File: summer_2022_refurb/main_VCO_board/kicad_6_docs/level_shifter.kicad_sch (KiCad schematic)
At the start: 5 parts

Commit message: Main VCO progress
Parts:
- removed R?: 100k, symbol Device:R
- R?: value 100k -> 33k
- R?: value 200k -> 100k
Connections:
- net GND: now also R?.1; no longer U?.3 (+)
- net IN: now also U?.3 (+); no longer R?.1
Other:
- note added: "Upgoing sawtooth [-1.25, +1.25v]"
- note added: "upgoing sawtooth [-5v, +5v]"
- note removed: "[-1.25, +1.25v] in"
- note removed: "[-5v, +5v] out"
- title: (none) -> Josh Ox Ribon Synth Main VCO board
- moved on the sheet: R?
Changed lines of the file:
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@@
 (kicad_sch (version 20211123) (generator eeschema)
   (paper "A4")
+  (title_block
+    (title "Josh Ox Ribon Synth Main VCO board")
+    (date "2022-06-18")
+    (rev "0")
+    (comment 2 "creativecommons.org/licences/by/4.0")
+    (comment 3 "license: CC by 4.0")
+    (comment 4 "Author: Jordan Acete")
+  )
   (junction (at 161.29 101.6) (diameter 0) (color 0 0 0 0)
   )
   (junction (at 161.29 91.44) (diameter 0) (color 0 0 0 0)
   )
-  (junction (at 135.89 101.6) (diameter 0) (color 0 0 0 0)
-  )
-  (junction (at 123.19 101.6) (diameter 0) (color 0 0 0 0)
-  )
-  (junction (at 140.97 101.6) (diameter 0) (color 0 0 0 0)
+  (junction (at 140.97 86.36) (diameter 0) (color 0 0 0 0)
   )
   (junction (at 140.97 91.44) (diameter 0) (color 0 0 0 0)
   )
-  (wire (pts (xy 135.89 96.52) (xy 135.89 101.6))
+  (wire (pts (xy 125.73 88.9) (xy 125.73 86.36))
     (stroke (width 0) (type default) (color 0 0 0 0))
   )
@@
     (stroke (width 0) (type default) (color 0 0 0 0))
   )
-  (wire (pts (xy 161.29 91.44) (xy 161.29 101.6))
+  (wire (pts (xy 135.89 86.36) (xy 140.97 86.36))
     (stroke (width 0) (type default) (color 0 0 0 0))
   )
-  (wire (pts (xy 135.89 101.6) (xy 140.97 101.6))
+  (wire (pts (xy 161.29 91.44) (xy 161.29 101.6))
     (stroke (width 0) (type default) (color 0 0 0 0))
   )
@@
     (stroke (width 0) (type default) (color 0 0 0 0))
   )
-  (wire (pts (xy 140.97 109.22) (xy 140.97 106.68))
-    (stroke (width 0) (type default) (color 0 0 0 0))
-  )
   (wire (pts (xy 140.97 101.6) (xy 143.51 101.6))
     (stroke (width 0) (type default) (color 0 0 0 0))
   )
-  (wire (pts (xy 123.19 101.6) (xy 123.19 96.52))
-    (stroke (width 0) (type default) (color 0 0 0 0))
-  )
-  (wire (pts (xy 140.97 80.01) (xy 140.97 91.44))
+  (wire (pts (xy 140.97 80.01) (xy 140.97 86.36))
     (stroke (width 0) (type default) (color 0 0 0 0))
   )
@@
     (stroke (width 0) (type default) (color 0 0 0 0))
   )
-  (wire (pts (xy 140.97 106.68) (xy 143.51 106.68))
+  (wire (pts (xy 105.41 106.68) (xy 143.51 106.68))
     (stroke (width 0) (type default) (color 0 0 0 0))
   )
-  (wire (pts (xy 133.35 106.68) (xy 135.89 106.68))
-    (stroke (width 0) (type default) (color 0 0 0 0))
-  )
-  (wire (pts (xy 95.25 101.6) (xy 123.19 101.6))
+  (wire (pts (xy 140.97 86.36) (xy 140.97 91.44))
     (stroke (width 0) (type default) (color 0 0 0 0))
   )
@@
     (stroke (width 0) (type default) (color 0 0 0 0))
   )
-  (wire (pts (xy 135.89 101.6) (xy 135.89 106.68))
-    (stroke (width 0) (type default) (color 0 0 0 0))
-  )
-  (wire (pts (xy 161.29 101.6) (xy 187.96 101.6))
+  (wire (pts (xy 161.29 101.6) (xy 195.58 101.6))
     (stroke (width 0) (type default) (color 0 0 0 0))
   )
@@
     (stroke (width 0) (type default) (color 0 0 0 0))
   )
-  (wire (pts (xy 125.73 106.68) (xy 123.19 106.68))
+  (wire (pts (xy 125.73 86.36) (xy 128.27 86.36))
     (stroke (width 0) (type default) (color 0 0 0 0))
   )
-  (wire (pts (xy 133.35 96.52) (xy 135.89 96.52))
-    (stroke (width 0) (type default) (color 0 0 0 0))
-  )
-  (wire (pts (xy 123.19 96.52) (xy 125.73 96.52))
-    (stroke (width 0) (type default) (color 0 0 0 0))
-  )
-  (wire (pts (xy 123.19 106.68) (xy 123.19 101.6))
-    (stroke (width 0) (type default) (color 0 0 0 0))
-  )
-  (text "[-1.25, +1.25v] in" (at 91.44 99.06 0)
+  (text "Upgoing sawtooth [-1.25, +1.25v]" (at 101.6 104.14 0)
     (effects (font (size 1.27 1.27)) (justify left bottom))
   )
-  (text "[-5v, +5v] out" (at 177.8 99.06 0)
+  (text "upgoing sawtooth [-5v, +5v]" (at 171.45 99.06 0)
     (effects (font (size 1.27 1.27)) (justify left bottom))
   )
-  (hierarchical_label "IN" (shape input) (at 95.25 101.6 180)
+  (hierarchical_label "IN" (shape input) (at 105.41 106.68 180)
     (effects (font (size 1.27 1.27)) (justify right))
   )
-  (hierarchical_label "OUT" (shape output) (at 187.96 101.6 0)
+  (hierarchical_label "OUT" (shape output) (at 195.58 101.6 0)
     (effects (font (size 1.27 1.27)) (justify left))
-  )
-  (symbol (lib_id "power:GND") (at 140.97 109.22 0) (unit 1)
-    (in_bom yes) (on_board yes) (fields_autoplaced)
-    (property "Reference" "#PWR?" (id 0) (at 140.97 115.57 0)
-      (effects (font (size 1.27 1.27)) hide)
-    )
-    (property "Value" "GND" (id 1) (at 140.97 114.3 0))
-    (property "Footprint" "" (id 2) (at 140.97 109.22 0)
-      (effects (font (size 1.27 1.27)) hide)
-    )
-    (property "Datasheet" "" (id 3) (at 140.97 109.22 0)
-      (effects (font (size 1.27 1.27)) hide)
-    )
-    (pin "1")
   )
   (symbol (lib_id "Amplifier_Operational:TL072") (at 151.13 104.14 0) (mirror x) (unit 1)
@@
     (pin "8")
   )
-  (symbol (lib_id "Device:R") (at 129.54 96.52 90) (unit 1)
+  (symbol (lib_id "Device:R") (at 132.08 86.36 90) (unit 1)
     (in_bom yes) (on_board yes) (fields_autoplaced)
-    (property "Reference" "R?" (id 0) (at 129.54 90.17 90))
-    (property "Value" "100k" (id 1) (at 129.54 92.71 90))
-    (property "Footprint" "" (id 2) (at 129.54 98.298 90)
+    (property "Reference" "R?" (id 0) (at 132.08 80.01 90))
+    (property "Value" "33k" (id 1) (at 132.08 82.55 90))
+    (property "Footprint" "" (id 2) (at 132.08 88.138 90)
       (effects (font (size 1.27 1.27)) hide)
     )
-    (property "Datasheet" "~" (id 3) (at 129.54 96.52 0)
+    (property "Datasheet" "~" (id 3) (at 132.08 86.36 0)
       (effects (font (size 1.27 1.27)) hide)
     )
     (pin "1")
     (pin "2")
+  )
+  (symbol (lib_id "power:GND") (at 125.73 88.9 0) (unit 1)
+    (in_bom yes) (on_board yes) (fields_autoplaced)
+    (property "Reference" "#PWR?" (id 0) (at 125.73 95.25 0)
+      (effects (font (size 1.27 1.27)) hide)
+    )
+    (property "Value" "GND" (id 1) (at 125.73 93.98 0))
+    (property "Footprint" "" (id 2) (at 125.73 88.9 0)
+      (effects (font (size 1.27 1.27)) hide)
+    )
+    (property "Datasheet" "" (id 3) (at 125.73 88.9 0)
+      (effects (font (size 1.27 1.27)) hide)
+    )
+    (pin "1")
   )
   (symbol (lib_id "Device:C") (at 151.13 80.01 90) (unit 1)
@@
     (pin "2")
   )
-  (symbol (lib_id "Device:R") (at 129.54 106.68 90) (unit 1)
-    (in_bom yes) (on_board yes) (fields_autoplaced)
-    (property "Reference" "R?" (id 0) (at 129.54 100.33 90))
-    (property "Value" "100k" (id 1) (at 129.54 102.87 90))
-    (property "Footprint" "" (id 2) (at 129.54 108.458 90)
-      (effects (font (size 1.27 1.27)) hide)
-    )
-    (property "Datasheet" "~" (id 3) (at 129.54 106.68 0)
-      (effects (font (size 1.27 1.27)) hide)
-    )
-    (pin "1")
-    (pin "2")
-  )
   (symbol (lib_id "Device:R") (at 151.13 91.44 90) (unit 1)
     (in_bom yes) (on_board yes) (fields_autoplaced)
     (property "Reference" "R?" (id 0) (at 151.13 85.09 90))
-    (property "Value" "200k" (id 1) (at 151.13 87.63 90))
+    (property "Value" "100k" (id 1) (at 151.13 87.63 90))
     (property "Footprint" "" (id 2) (at 151.13 93.218 90)
       (effects (font (size 1.27 1.27)) hide)

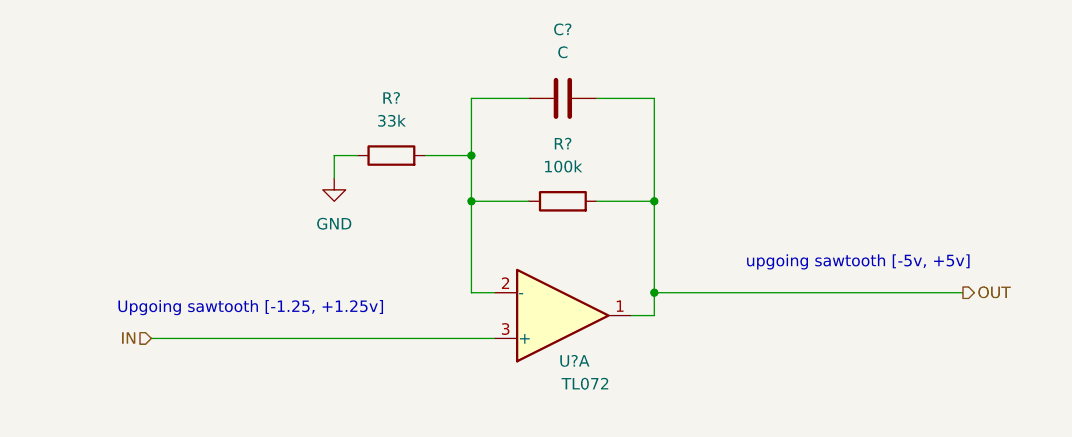
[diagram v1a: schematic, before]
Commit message: Progress on main VCO, schem getting close but not done
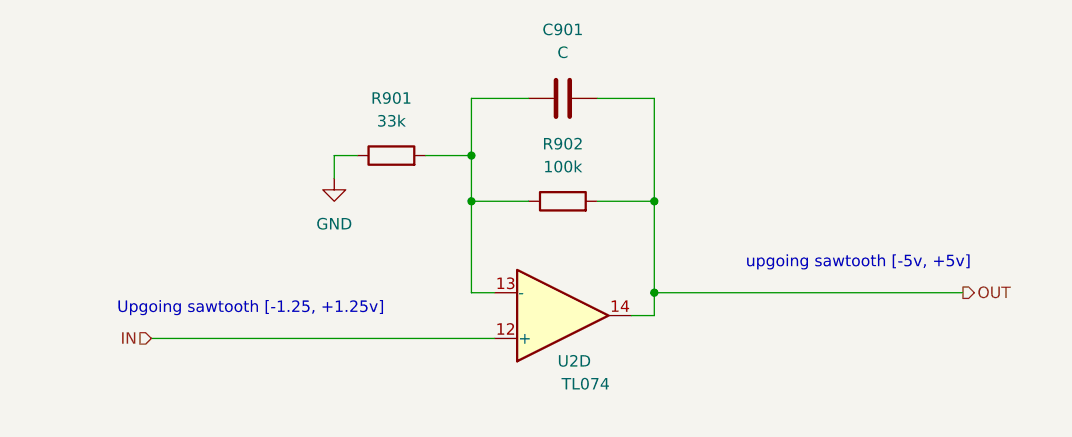
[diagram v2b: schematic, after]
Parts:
- removed U?: TL072, symbol Amplifier_Operational:TL072
- added U2: TL074, symbol Amplifier_Operational:TL074
- gave numbers to parts that had none: 3
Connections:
- net IN: now also U2.12 (+)
- net OUT: now also U2.14
- net at C901.1, R901.2, R902.1: now also U2.13 (-)
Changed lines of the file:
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@@
     (effects (font (size 1.27 1.27)) (justify left))
-  )
-  (symbol (lib_id "Amplifier_Operational:TL072") (at 151.13 104.14 0) (mirror x) (unit 1)
-    (in_bom yes) (on_board yes)
-    (property "Reference" "U?" (id 0) (at 152.4 109.22 0))
-    (property "Value" "TL072" (id 1) (at 153.67 111.76 0))
-    (property "Footprint" "" (id 2) (at 151.13 104.14 0)
-      (effects (font (size 1.27 1.27)) hide)
-    )
-    (property "Datasheet" "http://www.ti.com/lit/ds/symlink/tl071.pdf" (id 3) (at 151.13 104.14 0)
-      (effects (font (size 1.27 1.27)) hide)
-    )
-    (pin "1")
-    (pin "2")
-    (pin "3")
-    (pin "5")
-    (pin "6")
-    (pin "7")
-    (pin "4")
-    (pin "8")
   )
   (symbol (lib_id "Device:R") (at 132.08 86.36 90) (unit 1)
     (in_bom yes) (on_board yes) (fields_autoplaced)
-    (property "Reference" "R?" (id 0) (at 132.08 80.01 90))
+    (property "Reference" "R901" (id 0) (at 132.08 80.01 90))
     (property "Value" "33k" (id 1) (at 132.08 82.55 90))
     (property "Footprint" "" (id 2) (at 132.08 88.138 90)
@@
     (pin "2")
   )
+  (symbol (lib_id "Amplifier_Operational:TL074") (at 151.13 104.14 0) (mirror x) (unit 4)
+    (in_bom yes) (on_board yes)
+    (property "Reference" "U2" (id 0) (at 152.4 109.22 0))
+    (property "Value" "TL074" (id 1) (at 153.67 111.76 0))
+    (property "Footprint" "" (id 2) (at 149.86 106.68 0)
+      (effects (font (size 1.27 1.27)) hide)
+    )
+    (property "Datasheet" "http://www.ti.com/lit/ds/symlink/tl071.pdf" (id 3) (at 152.4 109.22 0)
+      (effects (font (size 1.27 1.27)) hide)
+    )
+    (pin "1")
+    (pin "2")
+    (pin "3")
+    (pin "5")
+    (pin "6")
+    (pin "7")
+    (pin "10")
+    (pin "8")
+    (pin "9")
+    (pin "12")
+    (pin "13")
+    (pin "14")
+    (pin "11")
+    (pin "4")
+  )
   (symbol (lib_id "power:GND") (at 125.73 88.9 0) (unit 1)
     (in_bom yes) (on_board yes) (fields_autoplaced)
-    (property "Reference" "#PWR?" (id 0) (at 125.73 95.25 0)
+    (property "Reference" "#PWR0901" (id 0) (at 125.73 95.25 0)
       (effects (font (size 1.27 1.27)) hide)
     )
@@
   (symbol (lib_id "Device:C") (at 151.13 80.01 90) (unit 1)
     (in_bom yes) (on_board yes) (fields_autoplaced)
-    (property "Reference" "C?" (id 0) (at 151.13 72.39 90))
+    (property "Reference" "C901" (id 0) (at 151.13 72.39 90))
     (property "Value" "C" (id 1) (at 151.13 74.93 90))
     (property "Footprint" "" (id 2) (at 154.94 79.0448 0)
@@
   (symbol (lib_id "Device:R") (at 151.13 91.44 90) (unit 1)
     (in_bom yes) (on_board yes) (fields_autoplaced)
-    (property "Reference" "R?" (id 0) (at 151.13 85.09 90))
+    (property "Reference" "R902" (id 0) (at 151.13 85.09 90))
     (property "Value" "100k" (id 1) (at 151.13 87.63 90))
     (property "Footprint" "" (id 2) (at 151.13 93.218 90)

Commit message: Main VCO rough parts placement
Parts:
- C901: footprint (none) -> Capacitor_SMD:C_0805_2012Metric
- R901, R902: footprint (none) -> Resistor_SMD:R_0805_2012Metric
- U2: footprint (none) -> Package_SO:SOIC-14_3.9x8.7mm_P1.27mm
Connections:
- net IN: now also U2.3 (+); no longer U2.12 (+)
- net OUT: now also U2.1; no longer U2.14
- net at C901.1, R901.2, R902.1: now also U2.2 (-); no longer U2.13 (-)
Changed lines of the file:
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@@
     (property "Reference" "R901" (id 0) (at 132.08 80.01 90))
     (property "Value" "33k" (id 1) (at 132.08 82.55 90))
-    (property "Footprint" "" (id 2) (at 132.08 88.138 90)
+    (property "Footprint" "Resistor_SMD:R_0805_2012Metric" (id 2) (at 132.08 88.138 90)
       (effects (font (size 1.27 1.27)) hide)
     )
@@
     (pin "2")
   )
-  (symbol (lib_id "Amplifier_Operational:TL074") (at 151.13 104.14 0) (mirror x) (unit 4)
+  (symbol (lib_id "Amplifier_Operational:TL074") (at 151.13 104.14 0) (mirror x) (unit 1)
     (in_bom yes) (on_board yes)
     (property "Reference" "U2" (id 0) (at 152.4 109.22 0))
     (property "Value" "TL074" (id 1) (at 153.67 111.76 0))
-    (property "Footprint" "" (id 2) (at 149.86 106.68 0)
+    (property "Footprint" "Package_SO:SOIC-14_3.9x8.7mm_P1.27mm" (id 2) (at 149.86 106.68 0)
       (effects (font (size 1.27 1.27)) hide)
     )
@@
     (property "Reference" "C901" (id 0) (at 151.13 72.39 90))
     (property "Value" "C" (id 1) (at 151.13 74.93 90))
-    (property "Footprint" "" (id 2) (at 154.94 79.0448 0)
+    (property "Footprint" "Capacitor_SMD:C_0805_2012Metric" (id 2) (at 154.94 79.0448 0)
       (effects (font (size 1.27 1.27)) hide)
     )
@@
     (property "Reference" "R902" (id 0) (at 151.13 85.09 90))
     (property "Value" "100k" (id 1) (at 151.13 87.63 90))
-    (property "Footprint" "" (id 2) (at 151.13 93.218 90)
+    (property "Footprint" "Resistor_SMD:R_0805_2012Metric" (id 2) (at 151.13 93.218 90)
       (effects (font (size 1.27 1.27)) hide)
     )

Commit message: Begin VCO pcb layout
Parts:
- renumbered U2 to U14
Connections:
- net IN: now also U14.10 (+); no longer U14.3 (+)
- net OUT: now also U14.8; no longer U14.1
- net at C901.1, R901.2, R902.1: now also U14.9 (-); no longer U14.2 (-)
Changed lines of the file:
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@@
     (pin "2")
   )
-  (symbol (lib_id "Amplifier_Operational:TL074") (at 151.13 104.14 0) (mirror x) (unit 1)
+  (symbol (lib_id "Amplifier_Operational:TL074") (at 151.13 104.14 0) (mirror x) (unit 3)
     (in_bom yes) (on_board yes)
-    (property "Reference" "U2" (id 0) (at 152.4 109.22 0))
+    (property "Reference" "U14" (id 0) (at 152.4 109.22 0))
     (property "Value" "TL074" (id 1) (at 153.67 111.76 0))
     (property "Footprint" "Package_SO:SOIC-14_3.9x8.7mm_P1.27mm" (id 2) (at 149.86 106.68 0)
